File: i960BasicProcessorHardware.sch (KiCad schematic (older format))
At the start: 74 parts, among them J1 Conn_01x08, J10 Conn_02x39_Odd_Even, J11 Conn_02x09_Odd_Even, J15 Conn_02x08_Odd_Even, J16 Conn_02x08_Odd_Even, J17 Conn_02x08_Odd_Even, J18 Conn_02x09_Odd_Even, J2 Conn_02x05_Odd_Even, J20 Conn_02x08_Odd_Even, J3 Conn_02x05_Odd_Even, J4 Conn_02x05_Odd_Even, J5 Conn_02x16_Odd_Even, J6 Conn_01x03, J7 Conn_01x03, J8 Conn_01x03, J9 Conn_01x11, U1 74HC245, U10 Adafruit_FeatherWing (PSRAM F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, U11 Adafruit_FeatherWing (PSRAM F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, U12 74LS125, U13 74LS04, U14 74LS08, U15 74LS174, U16 SN74LVC245AN, U17 74LS174, U2 80960Sx, U3 MCP23S17_SP, U4 MCP23S17_SP, U5 74HC245, U6 74HC573, U7 74HC573, U8 MCP23S17_SP, U9 MCP23S17_SP, X1 CXO_DIP14

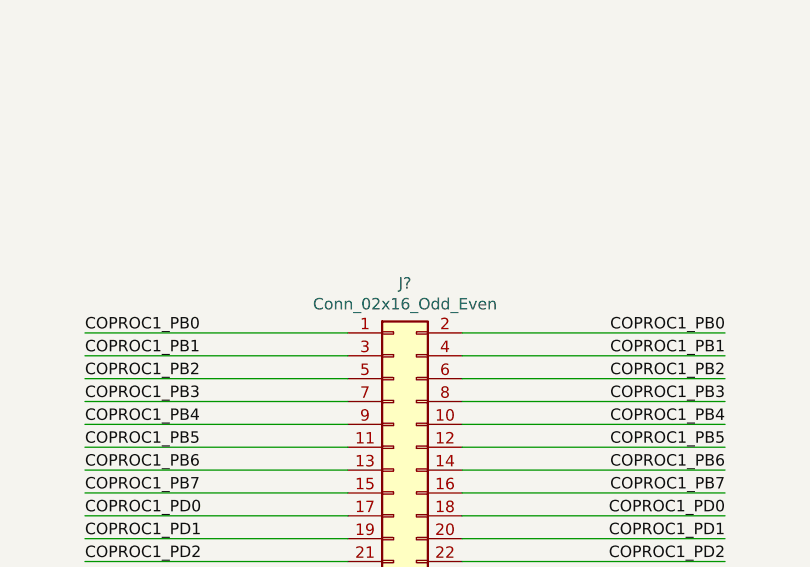
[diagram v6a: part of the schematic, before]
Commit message: Get the two co processors laid out properly and start wiring it up
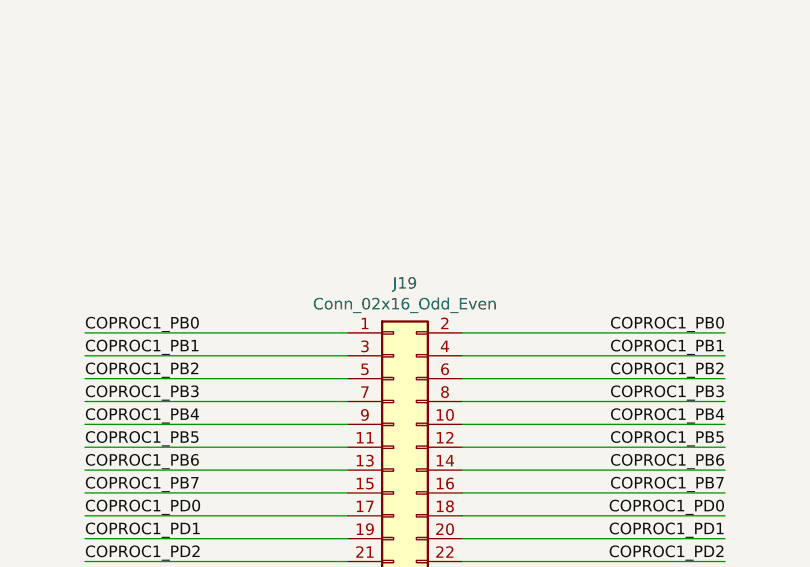
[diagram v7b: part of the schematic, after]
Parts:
- gave numbers to parts that had none: 1
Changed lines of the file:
@@
 COPROC1_PD7
 $Comp
-L Connector_Generic:Conn_02x16_Odd_Even J?
+L Connector_Generic:Conn_02x16_Odd_Even J19
 U 1 1 8791E5FC
 P 17700 7950
-F 0 "J?" H 17750 8867 50  0000 C CNN
+F 0 "J19" H 17750 8867 50  0000 C CNN
 F 1 "Conn_02x16_Odd_Even" H 17750 8776 50  0000 C CNN
 F 2 "Connector_PinHeader_2.54mm:PinHeader_2x16_P2.54mm_Vertical" H 17700 7950 50  0001 C CNN

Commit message: Finish cleaning up rev3 for now the layout is complete
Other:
- moved on the sheet: B1, J2, J3, J4
